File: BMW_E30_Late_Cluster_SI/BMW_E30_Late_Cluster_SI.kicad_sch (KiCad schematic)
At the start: 39 parts, among them J2 Coding Plug, J5 Nexus Connector, U1 ITT SAF1190-196 MCU, U2 ITT V3003-393, U3 ITT V3004-520, U5 LP2950-5.0_TO92, Y1 Crystal

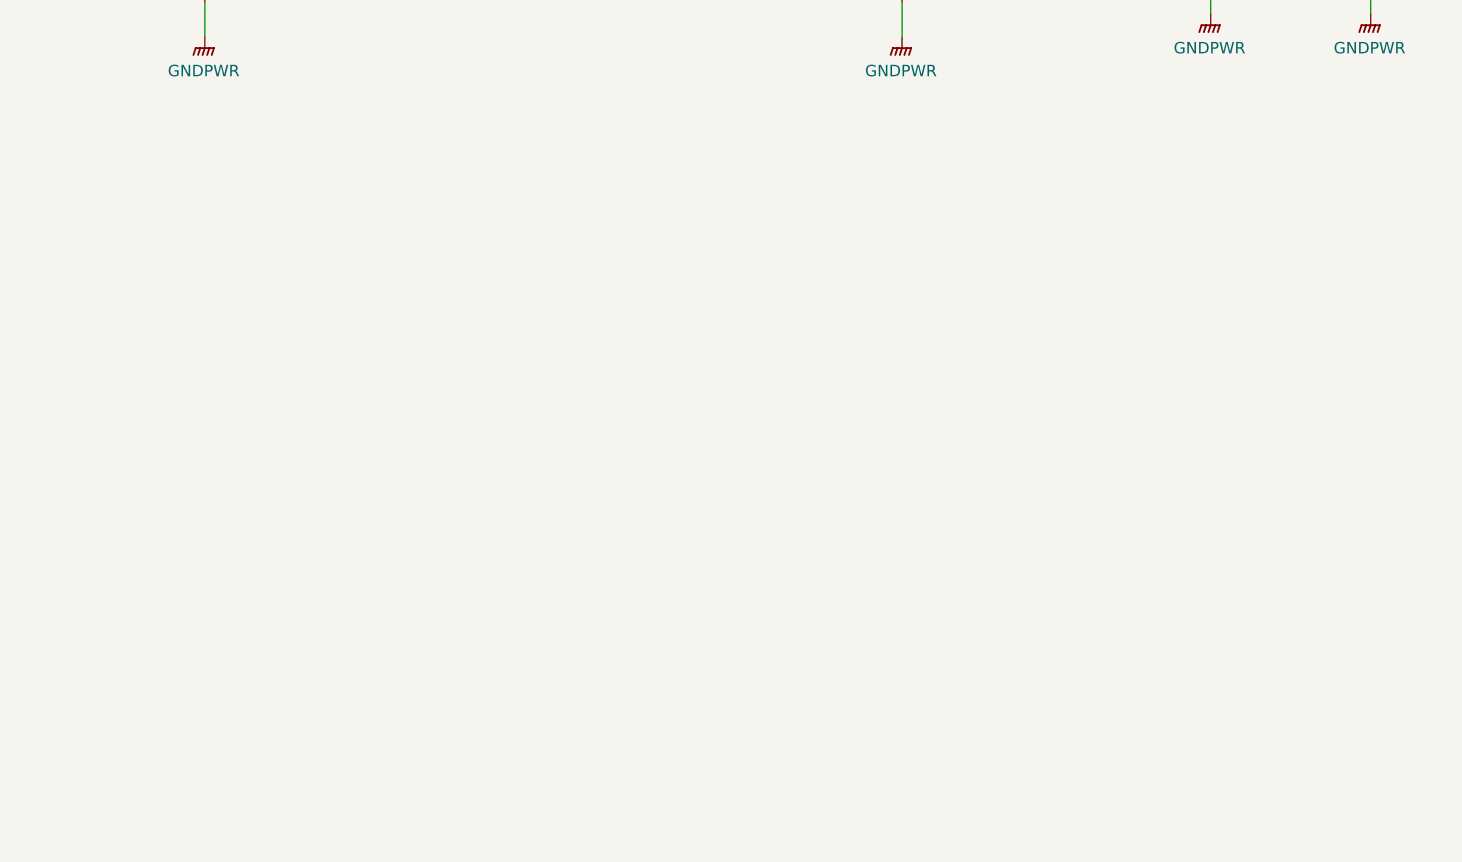
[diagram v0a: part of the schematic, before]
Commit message: SI layout updates
Component positions are mostly complete.
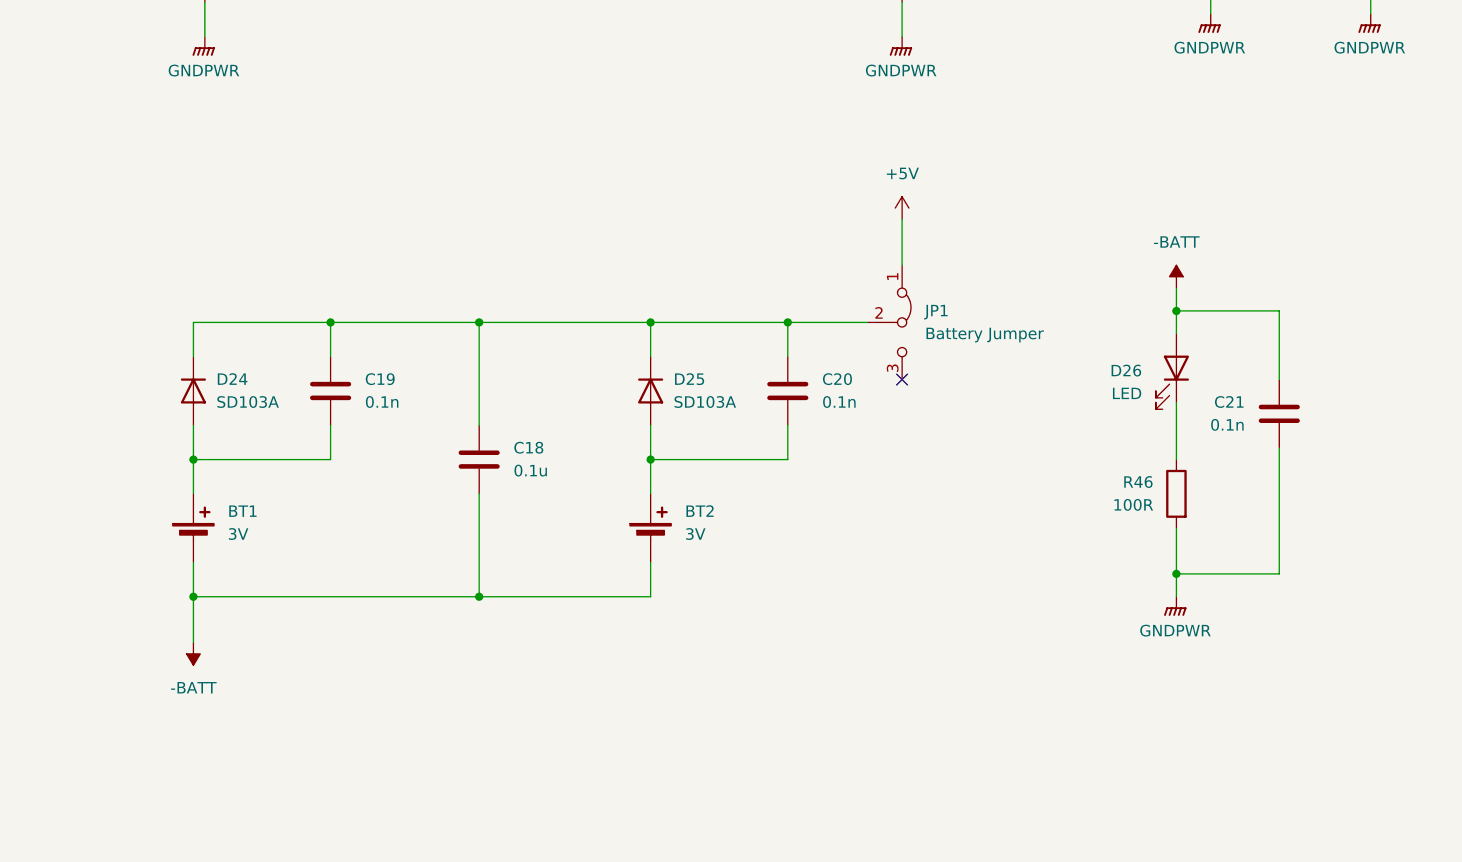
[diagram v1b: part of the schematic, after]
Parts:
- added BT1, BT2: 3V, SI_THT:Batt_CR14250SE, symbol Device:Battery_Cell
- added C18: 0.1u, Capacitor_THT:C_Rect_L7.0mm_W2.0mm_P5.00mm, symbol Device:C
- added C19, C20, C21: 0.1n, Capacitor_THT:C_Disc_D6.0mm_W2.5mm_P5.00mm, symbol Device:C
- added D24, D25: SD103A, SI_THT:D_Axial_Narrow_L6.7mm_D2.4mm_P9.7mm, symbol Device:D
- added D26: LED, LED_THT:LED_D3.0mm, symbol Device:LED
- added JP1: Battery Jumper, Connector_PinHeader_2.54mm:PinHeader_1x03_P2.54mm_Vertical, symbol Jumper:Jumper_3_Bridged12
- added R46: 100R, SI_THT:R_Axial_Narrow_L6.8mm_D2.4mm_P9.7mm, symbol Device:R
- D10, D5, D7: footprint (none) -> SI_THT:D_Axial_Narrow_L6.7mm_D2.4mm_P9.7mm
- D2, D3, D6, D9: footprint Diode_THT:D_DO-35_SOD27_P7.62mm_Horizontal -> SI_THT:D_Axial_Narrow_L6.7mm_D2.4mm_P9.7mm
- D4: footprint Diode_THT:D_DO-41_SOD81_P10.16mm_Horizontal -> SI_THT:D_Axial_Narrow_L6.7mm_D2.4mm_P9.7mm
- J2: footprint (none) -> Connector_PinSocket_2.54mm:PinSocket_1x08_P2.54mm_Horizontal
- J5: footprint BMW_Cluster_Connectors:E30_SI_Connector_Late_19Pin_P3.5 -> BMW_Cluster_Connectors:E30_Early_SI_Conn_Late_P3.5
- U2: footprint Package_DIP:DIP-16_W10.16mm_LongPads -> Package_DIP:DIP-18_W7.62mm_LongPads
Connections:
- net +5V: now also JP1.1 (A)
- net GNDPWR: now also C21.2, R46.2
- new net: D26.1 (K), R46.1
- new net: C18.1, C19.1, C20.1, D24.1 (K), D25.1 (K), JP1.2 (C)
- new net: BT2.1 (+), C20.2, D25.2 (A)
- new net: BT1.1 (+), C19.2, D24.2 (A)
- new net -BATT: BT1.2 (-), BT2.2 (-), C18.2, C21.1, D26.2 (A)
- no-connect marks 12 -> 13

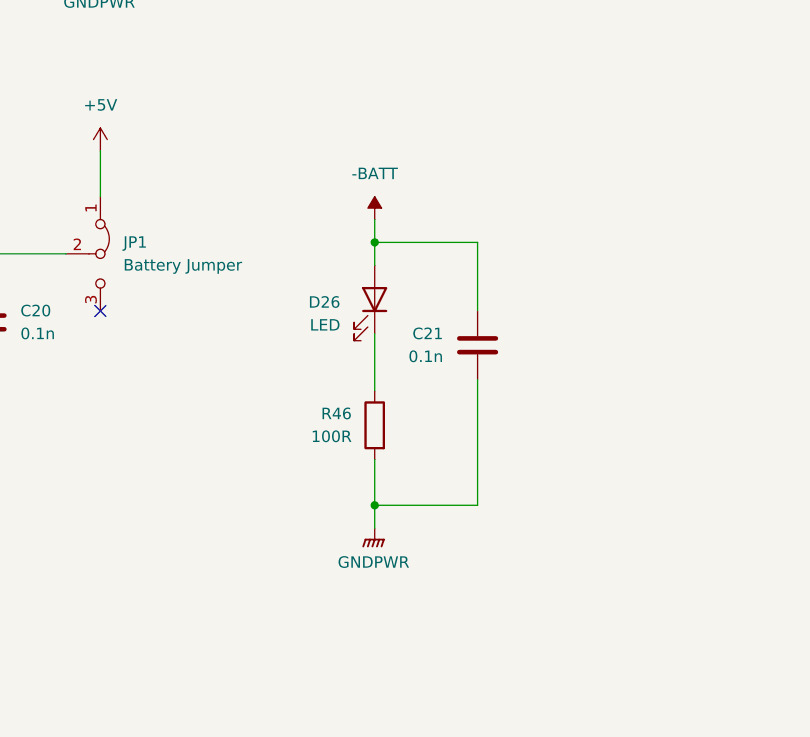
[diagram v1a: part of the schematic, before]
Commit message: Component Locations Generally Set
Component locations set up and ready for layout to begin.
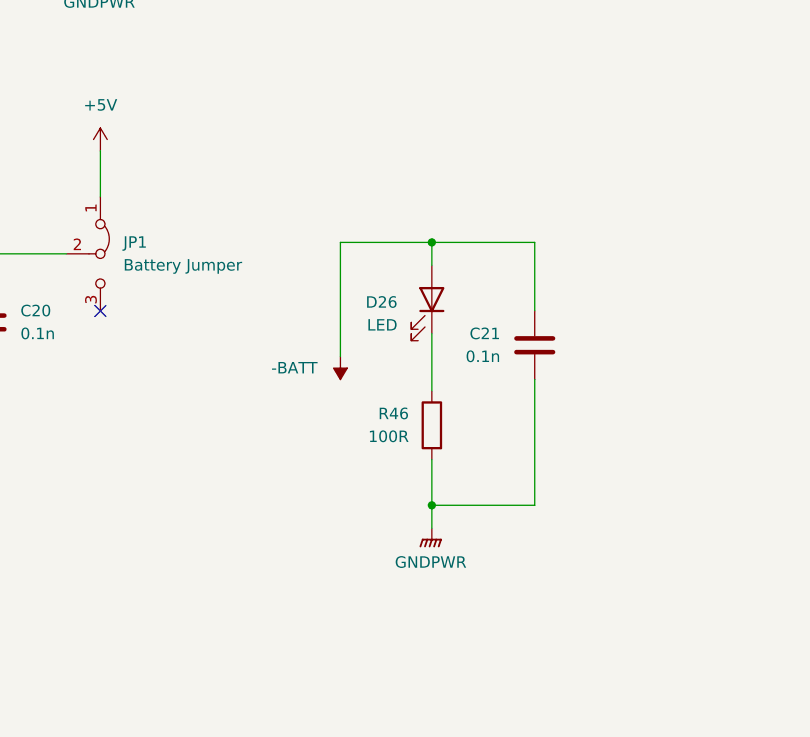
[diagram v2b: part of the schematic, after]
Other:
- moved on the sheet: C21, D26, R46
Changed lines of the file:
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@@
 	)
 	(junction
-		(at 204.47 93.98)
+		(at 210.82 93.98)
 		(diameter 0)
 		(color 0 0 0 0)
@@
 	)
 	(junction
-		(at 204.47 123.19)
+		(at 210.82 123.19)
 		(diameter 0)
 		(color 0 0 0 0)
@@
 	(wire
 		(pts
+			(xy 200.66 93.98) (xy 210.82 93.98)
+		)
+		(stroke
+			(width 0)
+			(type default)
+		)
+	)
+	(wire
+		(pts
 			(xy 34.29 46.99) (xy 39.37 46.99)
 		)
@@
 	(wire
 		(pts
-			(xy 215.9 101.6) (xy 215.9 93.98)
+			(xy 222.25 101.6) (xy 222.25 93.98)
 		)
 		(stroke
@@
 	(wire
 		(pts
-			(xy 204.47 93.98) (xy 204.47 96.52)
+			(xy 210.82 93.98) (xy 210.82 96.52)
 		)
 		(stroke
@@
 	(wire
 		(pts
-			(xy 204.47 104.14) (xy 204.47 110.49)
+			(xy 210.82 104.14) (xy 210.82 110.49)
 		)
 		(stroke
@@
 	(wire
 		(pts
-			(xy 215.9 93.98) (xy 204.47 93.98)
+			(xy 222.25 93.98) (xy 210.82 93.98)
 		)
 		(stroke
@@
 	(wire
 		(pts
-			(xy 204.47 91.44) (xy 204.47 93.98)
+			(xy 200.66 106.68) (xy 200.66 93.98)
 		)
 		(stroke
@@
 	(wire
 		(pts
-			(xy 204.47 123.19) (xy 204.47 125.73)
+			(xy 210.82 123.19) (xy 210.82 125.73)
 		)
 		(stroke
@@
 	(wire
 		(pts
-			(xy 215.9 123.19) (xy 204.47 123.19)
+			(xy 222.25 123.19) (xy 210.82 123.19)
 		)
 		(stroke
@@
 	(wire
 		(pts
-			(xy 215.9 109.22) (xy 215.9 123.19)
+			(xy 222.25 109.22) (xy 222.25 123.19)
 		)
 		(stroke
@@
 	(wire
 		(pts
-			(xy 204.47 118.11) (xy 204.47 123.19)
+			(xy 210.82 118.11) (xy 210.82 123.19)
 		)
 		(stroke
@@
 	(symbol
 		(lib_id "power:-BATT")
-		(at 204.47 91.44 0)
+		(at 200.66 106.68 0)
+		(mirror x)
 		(unit 1)
 		(exclude_from_sim no)
@@
 		(on_board yes)
 		(dnp no)
-		(fields_autoplaced yes)
 		(property "Reference" "#PWR053"
-			(at 204.47 95.25 0)
+			(at 200.66 102.87 0)
 			(effects
 				(font
@@
 		)
 		(property "Value" "-BATT"
-			(at 204.47 86.36 0)
+			(at 198.12 107.9499 0)
 			(effects
 				(font
 					(size 1.27 1.27)
 				)
+				(justify right)
 			)
 		)
 		(property "Footprint" ""
-			(at 204.47 91.44 0)
+			(at 200.66 106.68 0)
 			(effects
 				(font
@@
 		)
 		(property "Datasheet" ""
-			(at 204.47 91.44 0)
+			(at 200.66 106.68 0)
 			(effects
 				(font
@@
 		)
 		(property "Description" "Power symbol creates a global label with name \"-BATT\""
-			(at 204.47 91.44 0)
+			(at 200.66 106.68 0)
 			(effects
 				(font
@@
 	(symbol
 		(lib_id "Device:LED")
-		(at 204.47 100.33 270)
+		(at 210.82 100.33 270)
 		(mirror x)
 		(unit 1)
@@
 		(dnp no)
 		(property "Reference" "D26"
-			(at 200.66 100.6474 90)
+			(at 207.01 100.6474 90)
 			(effects
 				(font
@@
 		)
 		(property "Value" "LED"
-			(at 200.66 103.1874 90)
+			(at 207.01 103.1874 90)
 			(effects
 				(font
@@
 		)
 		(property "Footprint" "LED_THT:LED_D3.0mm"
-			(at 204.47 100.33 0)
+			(at 210.82 100.33 0)
 			(effects
 				(font
@@
 		)
 		(property "Datasheet" "~"
-			(at 204.47 100.33 0)
+			(at 210.82 100.33 0)
 			(effects
 				(font
@@
 		)
 		(property "Description" "Light emitting diode"
-			(at 204.47 100.33 0)
+			(at 210.82 100.33 0)
 			(effects
 				(font
@@
 		)
 		(property "Sim.Pins" "1=K 2=A"
-			(at 204.47 100.33 0)
+			(at 210.82 100.33 0)
 			(effects
 				(font
@@
 	(symbol
 		(lib_id "Device:C")
-		(at 215.9 105.41 0)
+		(at 222.25 105.41 0)
 		(mirror y)
 		(unit 1)
@@
 		(dnp no)
 		(property "Reference" "C21"
-			(at 212.09 104.1399 0)
+			(at 218.44 104.1399 0)
 			(effects
 				(font
@@
 		)
 		(property "Value" "0.1n"
-			(at 212.09 106.6799 0)
+			(at 218.44 106.6799 0)
 			(effects
 				(font
@@
 		)
 		(property "Footprint" "Capacitor_THT:C_Disc_D6.0mm_W2.5mm_P5.00mm"
-			(at 214.9348 109.22 0)
+			(at 221.2848 109.22 0)
 			(effects
 				(font
@@
 		)
 		(property "Datasheet" "~"
-			(at 215.9 105.41 0)
+			(at 222.25 105.41 0)
 			(effects
 				(font
@@
 		)
 		(property "Description" "Unpolarized capacitor"
-			(at 215.9 105.41 0)
+			(at 222.25 105.41 0)
 			(effects
 				(font
@@
 	(symbol
 		(lib_id "power:GNDPWR")
-		(at 204.47 125.73 0)
+		(at 210.82 125.73 0)
 		(unit 1)
 		(exclude_from_sim no)
@@
 		(fields_autoplaced yes)
 		(property "Reference" "#PWR050"
-			(at 204.47 130.81 0)
+			(at 210.82 130.81 0)
 			(effects
 				(font
@@
 		)
 		(property "Value" "GNDPWR"
-			(at 204.343 129.54 0)
+			(at 210.693 129.54 0)
 			(effects
 				(font
@@
 		)
 		(property "Footprint" ""
-			(at 204.47 127 0)
+			(at 210.82 127 0)
 			(effects
 				(font
@@
 		)
 		(property "Datasheet" ""
-			(at 204.47 127 0)
+			(at 210.82 127 0)
 			(effects
 				(font
@@
 		)
 		(property "Description" "Power symbol creates a global label with name \"GNDPWR\" , global ground"
-			(at 204.47 125.73 0)
+			(at 210.82 125.73 0)
 			(effects
 				(font
@@
 	(symbol
 		(lib_id "Device:R")
-		(at 204.47 114.3 0)
+		(at 210.82 114.3 0)
 		(mirror y)
 		(unit 1)
@@
 		(dnp no)
 		(property "Reference" "R46"
-			(at 201.93 113.0299 0)
+			(at 208.28 113.0299 0)
 			(effects
 				(font
@@
 		)
 		(property "Value" "100R"
-			(at 201.93 115.5699 0)
+			(at 208.28 115.5699 0)
 			(effects
 				(font
@@
 		)
 		(property "Footprint" "SI_THT:R_Axial_Narrow_L6.8mm_D2.4mm_P9.7mm"
-			(at 206.248 114.3 90)
+			(at 212.598 114.3 90)
 			(effects
 				(font
@@
 		)
 		(property "Datasheet" "~"
-			(at 204.47 114.3 0)
+			(at 210.82 114.3 0)
 			(effects
 				(font
@@
 		)
 		(property "Description" "5%"
-			(at 204.47 114.3 0)
+			(at 210.82 114.3 0)
 			(effects
 				(font

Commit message: SI Board Layout Updates
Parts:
- R44: footprint SI_THT:R_Axial_Narrow_L6.8mm_D2.4mm_P9.7mm -> SI_THT:R_Axial_Narrow_L6.8mm_D2.4mm_P22.4mm
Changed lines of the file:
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@@
 			)
 		)
-		(property "Footprint" "SI_THT:R_Axial_Narrow_L6.8mm_D2.4mm_P9.7mm"
+		(property "Footprint" "SI_THT:R_Axial_Narrow_L6.8mm_D2.4mm_P22.4mm"
 			(at 59.182 264.16 90)
 			(effects

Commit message: SI Board Layout Complete
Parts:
- added C10: 68n, Capacitor_THT:C_Disc_D6.0mm_W2.5mm_P5.00mm, symbol Device:C
- added JP10, JP11, JP12, JP2, JP3, JP4, JP5, JP6, JP7, JP8, JP9: Jumper, SI_THT:Jumper_THT_P9.7mm, symbol Jumper:Jumper_2_Bridged
- renumbered JP1 to JP20
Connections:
- net +5V: now also JP12.1 (A); no longer JP20.1 (A)
- net GNDPWR: now also U3.22, C10.2, JP10.1 (A), JP10.2 (B), JP3.1 (A); no longer U1.21
- net IC1_P22: now also JP2.1 (A); no longer U1.22
- net IC1_P35: now also JP11.1 (A); no longer U1.35
- net IC2_P11: now also JP7.2 (B); no longer R45.2, Y1.2
- net IC2_P12: now also JP9.1 (A); no longer R45.1, Y1.1
- net IC3_P7: now also JP4.1 (A); no longer U2.1
- new net: JP3.2 (B), U1.21
- new net: JP2.2 (B), U1.22
- new net: JP11.2 (B), U1.35
- new net: JP4.2 (B), JP5.1 (A)
- new net: JP8.1 (A), JP9.2 (B)
- new net: JP8.2 (B), R45.1, Y1.1
- new net: JP12.2 (B), JP20.1 (A)
- new net: JP6.1 (A), JP7.1 (A)
- new net: JP6.2 (B), R45.2, Y1.2
- new net IC2_P1: C10.1, JP5.2 (B), U2.1
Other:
- moved on the sheet: C5, D9, R2, R42, R43, R44, R45, R7, R8, U1, U2, U3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

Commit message: Readability Improvements
Organized the schematic for better readability, also made a few minor adjustments to the layout for simplicity.
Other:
- note added: "ASICs"
- note added: "Battery Charging"
- note added: "Interfaces"
- note added: "Jumpers for Routing"
- note added: "Power Supply"
- note added: "SI Data Inputs"
- moved on the sheet: C10, C5, JP10, JP12, JP4, JP5, JP6, JP7, JP8, JP9, R2, R42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

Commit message: Updates for GBR files
Slight stylistic improvements for GBR files as well as added some links to parts on digikey.
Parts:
- J2: Vendor Link (none) -> https://www.digikey.com/en/products/detail/sullins-connecto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
